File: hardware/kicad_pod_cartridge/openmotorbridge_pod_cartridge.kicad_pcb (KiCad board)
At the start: 2 copper layers, 35 x 25 mm, 4 parts, among them J1 POGO_6PIN, U1 DS2401

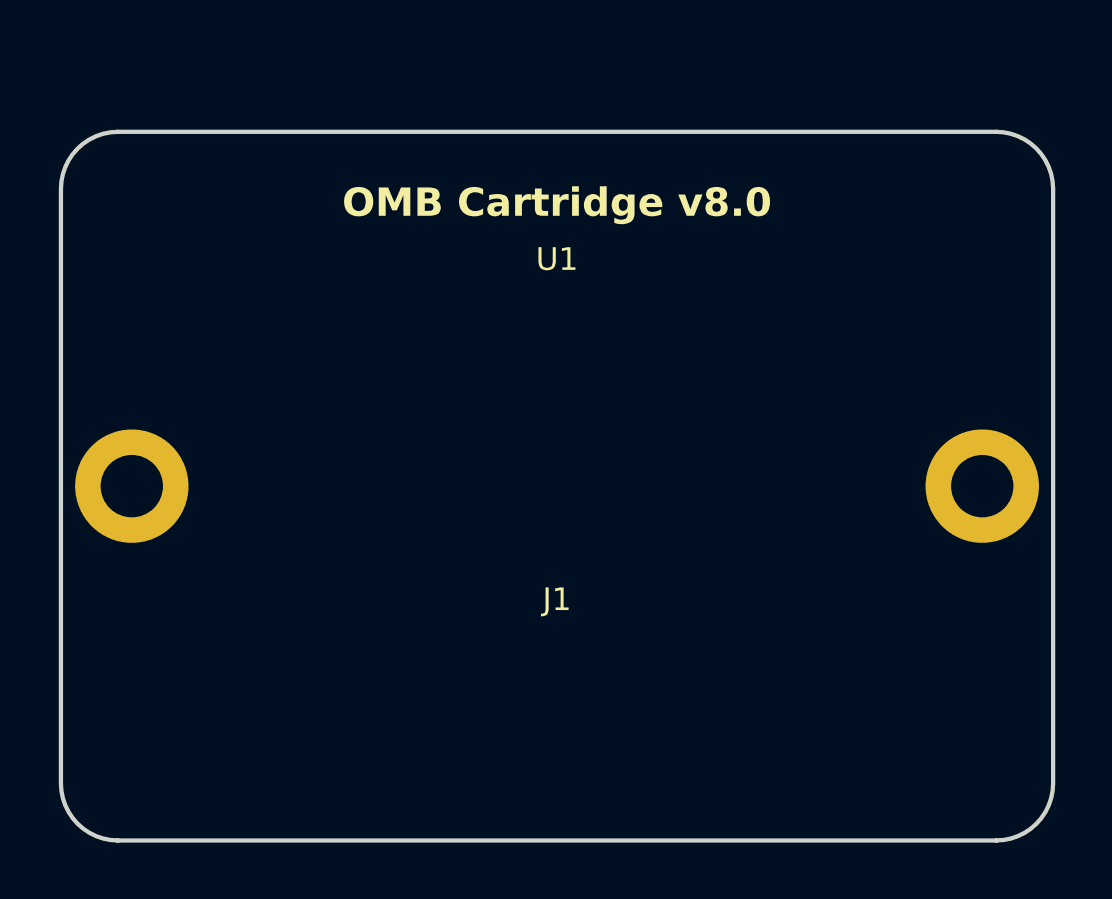
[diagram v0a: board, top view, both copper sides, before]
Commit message: feat(hardware,firmware): integrate OMM UART push flashing, low-profile cartridge & pod3 6-pin layout
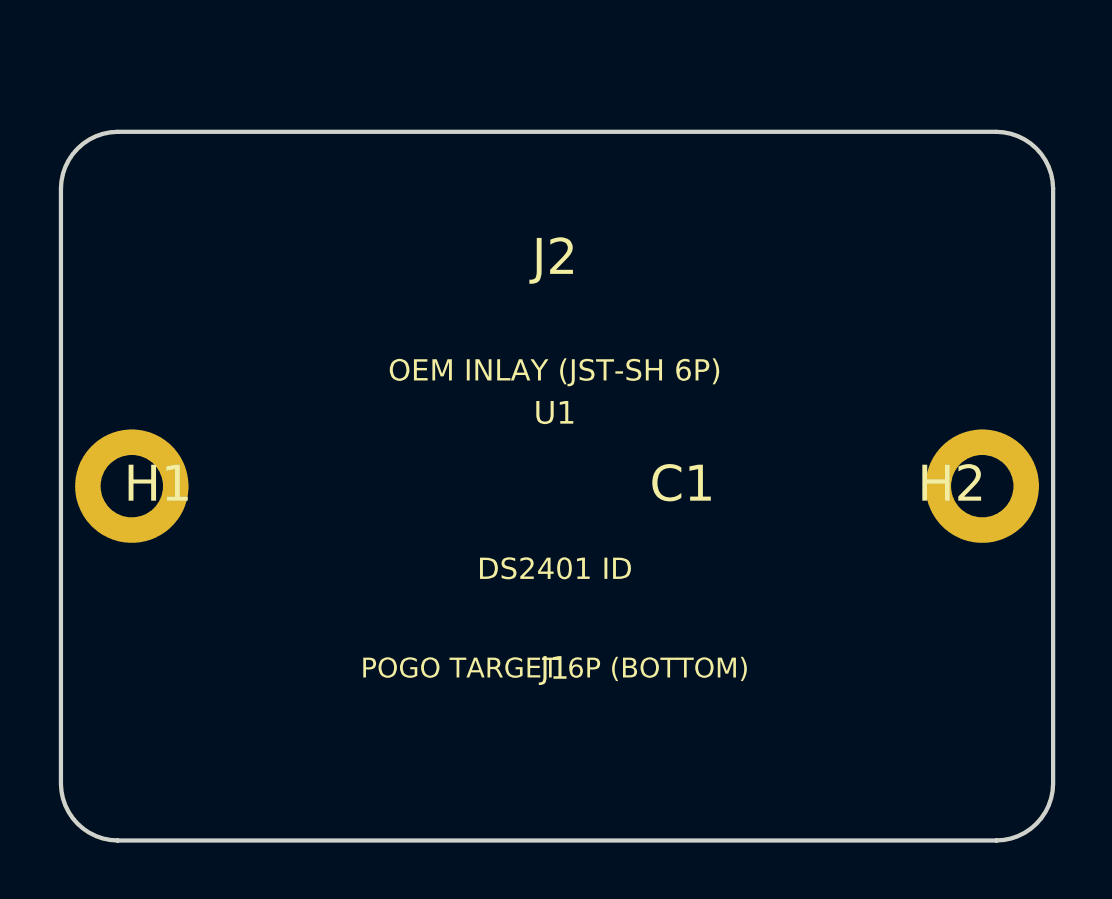
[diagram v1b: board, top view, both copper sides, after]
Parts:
- added C1: , , F.Cu at (122.0, 82.5)
- added H1: , , F.Cu at (103.5, 82.5)
- added H2: , , F.Cu at (131.5, 82.5)
- added J2: , , F.Cu at (117.5, 74.5)
- moved U1 5.43 mm to (117.5, 82.5)
- moved J1 2.43 mm to (117.5, 91.5)
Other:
- board text added: "DS2401 ID"
- board text added: "OEM INLAY (JST-SH 6P)"
- board text added: "POGO TARGET 6P (BOTTOM)"
- board text removed: "OMB Cartridge v8.0"
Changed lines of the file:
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@@
+		)
+	)
+	(footprint ""
+		(layer "F.Cu")
+		(at 131.5 82.5)
+		(property "Reference" "H2"
+			(at 0 0 0)
+			(layer "F.SilkS")
+			(effects
+				(font
+					(size 1.27 1.27)
+				)
+			)
+		)
+		(property "Value" ""
+			(at 0 0 0)
+			(layer "F.Fab")
+			(effects
+				(font
+					(size 1.27 1.27)
+				)
+			)
+		)
+		(property "Datasheet" ""
+			(at 0 0 0)
+			(layer "F.Fab")
+			(hide yes)
+			(effects
+				(font
+					(size 1.27 1.27)
+				)
+			)
+		)
+		(property "Description" ""
+			(at 0 0 0)
+			(layer "F.Fab")
+			(hide yes)
+			(effects
+				(font
+					(size 1.27 1.27)
+				)
+			)
+		)
+		(duplicate_pad_numbers_are_jumpers no)
+		(embedded_fonts no)
+	)
+	(footprint ""
+		(layer "F.Cu")
+		(at 122 82.5)
+		(property "Reference" "C1"
+			(at 0 0 0)
+			(layer "F.SilkS")
+			(effects
+				(font
+					(size 1.27 1.27)
+				)
+			)
+		)
+		(property "Value" ""
+			(at 0 0 0)
+			(layer "F.Fab")
+			(effects
+				(font
+					(size 1.27 1.27)
+				)
+			)
+		)
+		(property "Datasheet" ""
+			(at 0 0 0)
+			(layer "F.Fab")
+			(hide yes)
+			(effects
+				(font
+					(size 1.27 1.27)
+				)
+			)
+		)
+		(property "Description" ""
+			(at 0 0 0)
+			(layer "F.Fab")
+			(hide yes)
+			(effects
+				(font
+					(size 1.27 1.27)
+				)
+			)
+		)
+		(duplicate_pad_numbers_are_jumpers no)
+		(embedded_fonts no)
+		(model "${KICAD10_3DMODEL_DIR}/Capacitor_SMD.3dshapes/C_0603_1608Metric.step"
+			(offset
+				(xyz 0 0 0)
+			)
+			(scale
+				(xyz 1 1 1)
+			)
+			(rotate
+				(xyz 0 0 0)
+			)
 		)
 	)
@@
 	(footprint "Connector_PinHeader_2.54mm:PinHeader_1x06_P2.54mm_Vertical"
 		(layer "F.Cu")
-		(at 117.575 89.075)
+		(at 117.5 91.5)
 		(property "Reference" "J1"
 			(at 0 -2.5 0)
@@
 		(duplicate_pad_numbers_are_jumpers no)
 		(embedded_fonts no)
-		(model "/Connector_PinHeader_2.54mm.3dshapes/PinHeader_1x06_P2.54mm_Vertical.step"
+		(model "${KICAD10_3DMODEL_DIR}/Connector_PinHeader_2.54mm.3dshapes/PinHeader_1x06_P2.54mm_Horizontal.step"
 			(offset
 				(xyz 0 0 0)
@@
 			)
 			(rotate
-				(xyz 0 0 0)
-			)
-		)
+				(xyz 0 0 90)
+			)
+		)
+	)
+	(footprint ""
+		(layer "F.Cu")
+		(at 117.5 74.5)
+		(property "Reference" "J2"
+			(at 0 0 0)
+			(layer "F.SilkS")
+			(effects
+				(font
+					(size 1.27 1.27)
+				)
+			)
+		)
+		(property "Value" ""
+			(at 0 0 0)
+			(layer "F.Fab")
+			(effects
+				(font
+					(size 1.27 1.27)
+				)
+			)
+		)
+		(property "Datasheet" ""
+			(at 0 0 0)
+			(layer "F.Fab")
+			(hide yes)
+			(effects
+				(font
+					(size 1.27 1.27)
+				)
+			)
+		)
+		(property "Description" ""
+			(at 0 0 0)
+			(layer "F.Fab")
+			(hide yes)
+			(effects
+				(font
+					(size 1.27 1.27)
+				)
+			)
+		)
+		(duplicate_pad_numbers_are_jumpers no)
+		(embedded_fonts no)
+		(model "${KICAD10_3DMODEL_DIR}/Connector_JST.3dshapes/JST_SH_SM06B-SRSS-TB_1x06-1MP_P1.00mm_Horizontal.step"
+			(offset
+				(xyz 0 0 0)
+			)
+			(scale
+				(xyz 1 1 1)
+			)
+			(rotate
+				(xyz 0 0 0)
+			)
+		)
+	)
+	(footprint ""
+		(layer "F.Cu")
+		(at 103.5 82.5)
+		(property "Reference" "H1"
+			(at 0 0 0)
+			(layer "F.SilkS")
+			(effects
+				(font
+					(size 1.27 1.27)
+				)
+			)
+		)
+		(property "Value" ""
+			(at 0 0 0)
+			(layer "F.Fab")
+			(effects
+				(font
+					(size 1.27 1.27)
+				)
+			)
+		)
+		(property "Datasheet" ""
+			(at 0 0 0)
+			(layer "F.Fab")
+			(hide yes)
+			(effects
+				(font
+					(size 1.27 1.27)
+				)
+			)
+		)
+		(property "Description" ""
+			(at 0 0 0)
+			(layer "F.Fab")
+			(hide yes)
+			(effects
+				(font
+					(size 1.27 1.27)
+				)
+			)
+		)
+		(duplicate_pad_numbers_are_jumpers no)
+		(embedded_fonts no)
 	)
 	(footprint "MountingHole:MountingHole_2.2mm_M2"
@@
 	(footprint "Package_TO_SOT_SMD:SOT-23"
 		(layer "F.Cu")
-		(at 117.575 77.075)
+		(at 117.5 82.5)
 		(property "Reference" "U1"
 			(at 0 -2.5 0)
@@
 		(duplicate_pad_numbers_are_jumpers no)
 		(embedded_fonts no)
-		(model "/Package_TO_SOT_SMD.3dshapes/SOT-23.step"
+		(model "${KICAD10_3DMODEL_DIR}/Package_TO_SOT_SMD.3dshapes/SOT-23.step"
 			(offset
 				(xyz 0 0 0)
@@
 		(layer "Edge.Cuts")
 	)
-	(gr_text "OMB Cartridge v8.0"
-		(at 117.575 72.575 0)
+	(gr_text "POGO TARGET 6P (BOTTOM)"
+		(at 117.5 89 0)
 		(layer "F.SilkS")
 		(effects
 			(font
-				(size 1 1)
-				(thickness 0.15)
-				(bold yes)
-			)
-		)
+				(size 0.7 0.7)
+				(thickness 0.13)
+			)
+		)
+	)
+	(gr_text "OEM INLAY (JST-SH 6P)"
+		(at 117.5 78.5 0)
+		(layer "F.SilkS")
+		(effects
+			(font
+				(size 0.75 0.75)
+				(thickness 0.14)
+			)
+		)
+	)
+	(gr_text "DS2401 ID"
+		(at 117.5 85.5 0)
+		(layer "F.SilkS")
+		(effects
+			(font
+				(size 0.75 0.75)
+				(thickness 0.14)
+			)
+		)

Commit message: fix(hardware): rotate J2 horizontal connector outward on Pod Cartridge for direct straight-in cable entry
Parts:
- turned J2 to 180 degrees
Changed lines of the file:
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@@
 	(footprint ""
 		(layer "F.Cu")
-		(at 117.5 74.5)
+		(at 117.5 74.5 180)
 		(property "Reference" "J2"
-			(at 0 0 0)
+			(at 0 0 180)
 			(layer "F.SilkS")
 			(effects
@@
 		)
 		(property "Value" ""
-			(at 0 0 0)
+			(at 0 0 180)
 			(layer "F.Fab")
 			(effects
@@
 		)
 		(property "Datasheet" ""
-			(at 0 0 0)
+			(at 0 0 180)
 			(layer "F.Fab")
 			(hide yes)
@@
 		)
 		(property "Description" ""
-			(at 0 0 0)
+			(at 0 0 180)
 			(layer "F.Fab")
 			(hide yes)

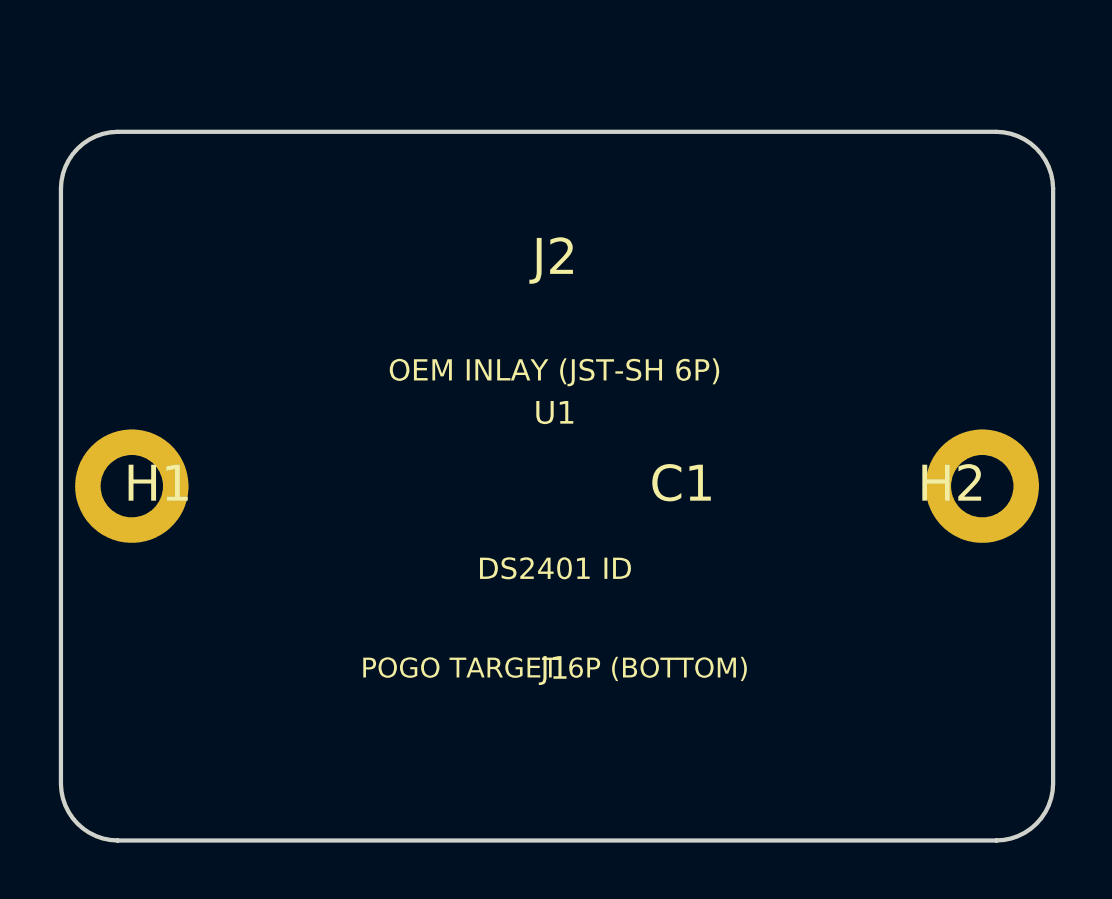
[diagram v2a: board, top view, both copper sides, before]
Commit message: feat(hardware): adapt pod cartridge carrier PCB with left stirnwand pogo pads and low-profile JST-SH header
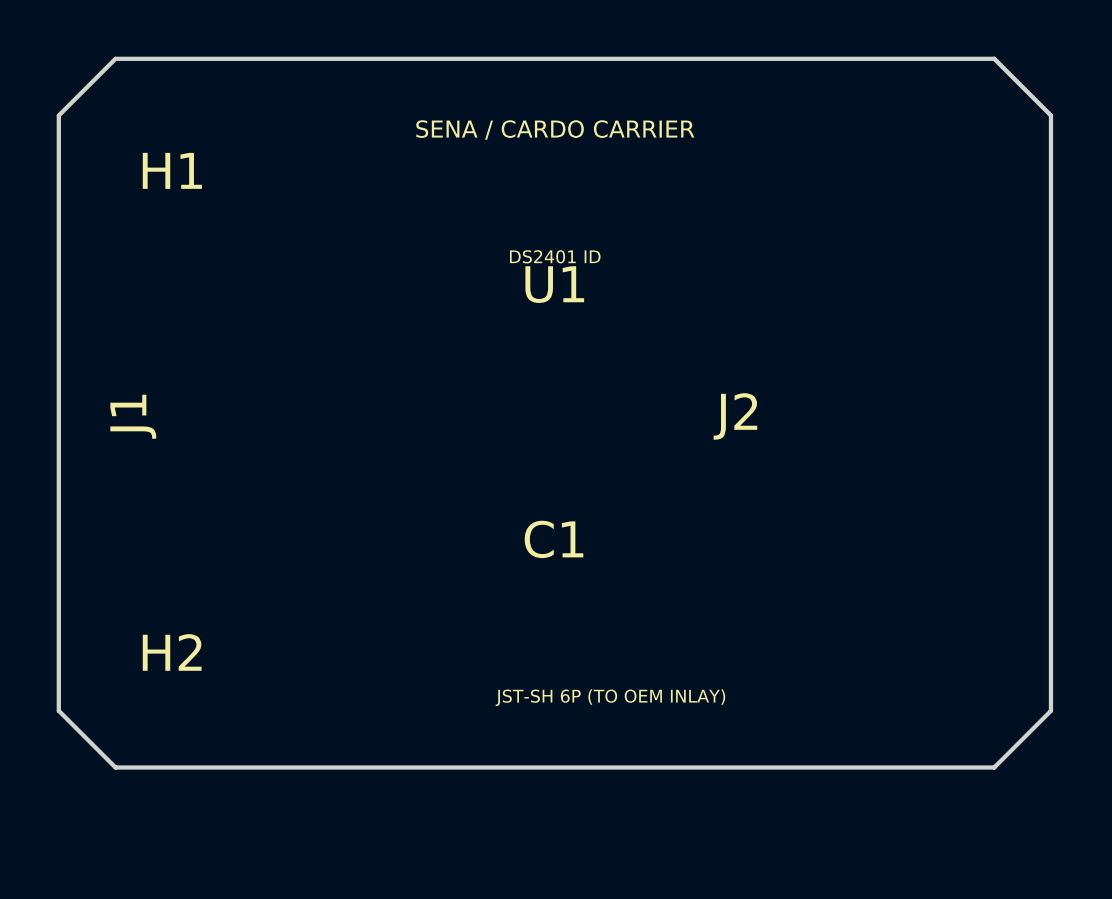
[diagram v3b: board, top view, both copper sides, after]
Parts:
- removed ? (x2): , MountingHole:MountingHole_2.2mm_M2
- J1: value POGO_6PIN -> (none); footprint Connector_PinHeader_2.54mm:PinHeader_1x06_P2.54mm_Vertical -> (none)
- U1: value DS2401 -> (none); footprint Package_TO_SOT_SMD:SOT-23 -> (none)
- moved H2 28.1 mm to (104.0, 88.5)
- moved J1 18.9 mm to (102.5, 80.0), turned to 90 degrees
- moved H1 11.0 mm to (104.0, 71.5)
- moved J2 8.51 mm to (124.0, 80.0), turned to 0 degrees
- moved U1 7.00 mm to (117.5, 75.5)
- moved C1 4.92 mm to (117.5, 84.5)
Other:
- board text added: "JST-SH 6P (TO OEM INLAY)"
- board text added: "SENA / CARDO CARRIER"
- board text removed: "OEM INLAY (JST-SH 6P)"
- board text removed: "POGO TARGET 6P (BOTTOM)"

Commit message: feat(hardware): configure cartridge PCB with bottom-facing 6-pin socket and top 90-degree JST-SH header for Sena/Cardo
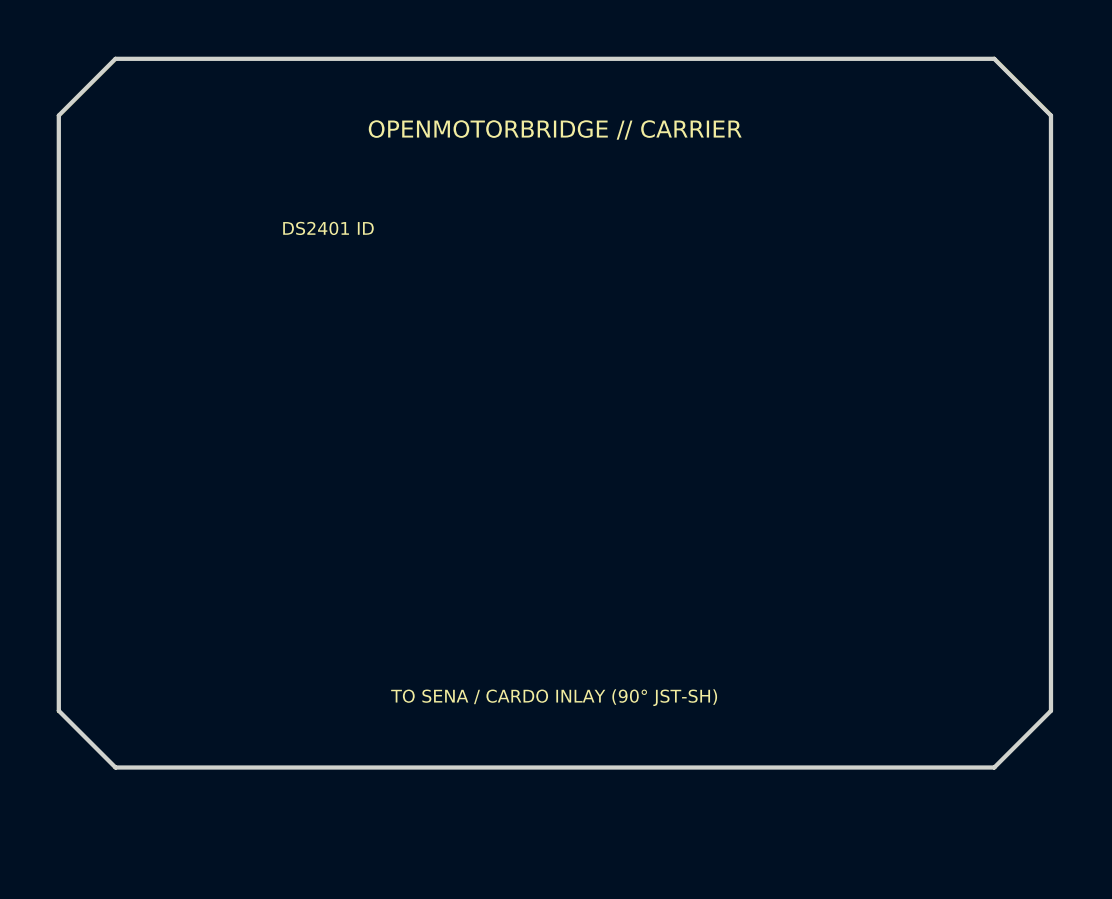
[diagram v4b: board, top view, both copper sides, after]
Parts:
- J1: moved to B.Cu
- moved H2 28.8 mm to (131.5, 80.0)
- moved J1 15.0 mm to (117.5, 80.0), turned to 0 degrees
- moved H1 8.51 mm to (103.5, 80.0)
- moved C1 8.06 mm to (109.5, 83.5)
- moved U1 8.06 mm to (109.5, 76.5)
- moved J2 1.50 mm to (125.5, 80.0), turned to 90 degrees
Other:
- board text added: "6-PIN SOCKET (MATES TO POD-BASE)"
- board text added: "GND SHIELD PLANE"
- board text added: "OPENMOTORBRIDGE // CARRIER"
- board text added: "TO SENA / CARDO INLAY (90° JST-SH)"
- board text removed: "JST-SH 6P (TO OEM INLAY)"
- board text removed: "SENA / CARDO CARRIER"

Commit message: feat(hardware): add 500mA PTC fuse F1, green power LED D1, resistor R1 on cartridge carrier PCB
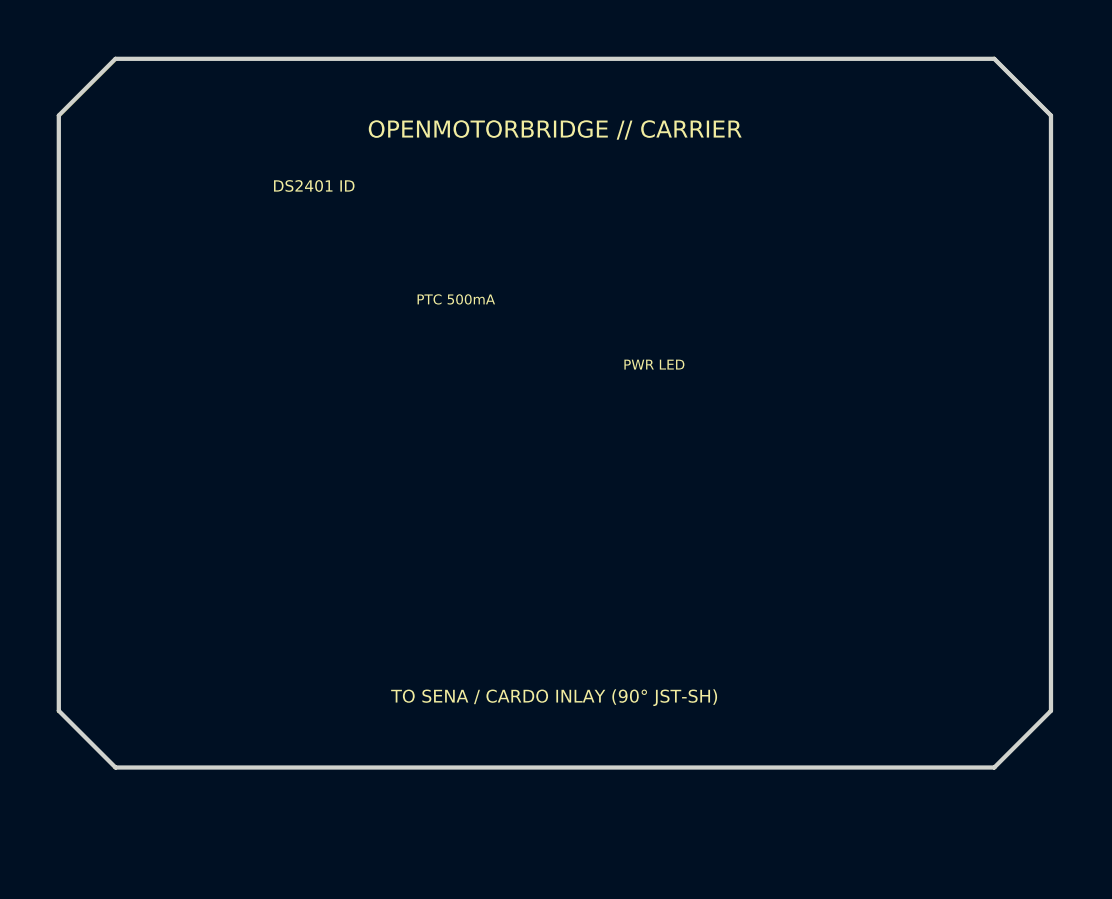
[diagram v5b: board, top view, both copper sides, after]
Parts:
- added D1: , , F.Cu at (121.0, 73.5)
- added F1: , , F.Cu at (114.0, 73.5)
- added R1: , , F.Cu at (121.0, 76.0)
- moved C1 1.12 mm to (109.0, 84.5)
- moved U1 1.12 mm to (109.0, 75.5)
- moved J2 0.50 mm to (126.0, 80.0)
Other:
- board text added: "PTC 500mA"
- board text added: "PWR LED"
